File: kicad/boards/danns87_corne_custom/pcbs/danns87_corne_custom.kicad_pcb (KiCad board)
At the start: 2 copper layers, 130.4 x 81.3 mm, 46 parts

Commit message: danns87_corne_custom: PCB tracks added, DRC passes with warnings, and, I think, ready for mfg
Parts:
- removed ?: , Button_Switch_SMD:SW_SPDT_PCM12
- removed ?: , Button_Switch_SMD:SW_SPST_UXCELL
- added S22: , Button_Switch_SMD:SW_SPST_UXCELL, F.Cu at (130.8, -10.6)
- added T1: , Button_Switch_SMD:SW_SPDT_PCM12, F.Cu at (126.9, -49.7)
- gave numbers to parts that had none: 1
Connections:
- D10 pad 1: middle_bottom -> P6
- D10 pad 2: P6 -> middle_bottom
- D11 pad 1: middle_home -> P5
- D11 pad 2: P5 -> middle_home
- D12 pad 1: middle_top -> P4
- D12 pad 2: P4 -> middle_top
- D13 pad 1: index_bottom -> P6
- D13 pad 2: P6 -> index_bottom
- D14 pad 2: P5 -> index_home
- D15 pad 2: P4 -> index_top
- D16 pad 2: P6 -> inner_bottom
- D17 pad 1: inner_home -> P5
- D17 pad 2: P5 -> inner_home
- D19 pad 1: near_thumb -> P7
- D19 pad 2: P7 -> near_thumb
- D20 pad 1: home_thumb -> P7
- D20 pad 2: P7 -> home_thumb
- D21 pad 2: P7 -> far_thumb
- D3 pad 1: outer_top -> P4
- D3 pad 2: P4 -> outer_top
- D4 pad 1: pinky_bottom -> P6
- D5 pad 1: pinky_home -> P5
- D5 pad 2: P5 -> pinky_home
- D6 pad 1: pinky_top -> P4
- D6 pad 2: P4 -> pinky_top
- D7 pad 1: ring_bottom -> P6
- D8 pad 1: ring_home -> P5
- D8 pad 2: P5 -> ring_home
- D9 pad 2: P4 -> ring_top
- S1 pad 2: P14 -> P21
- S2 pad 2: P14 -> P21
- S3 pad 2: P14 -> P21
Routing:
- net P6: track 0.00 -> 244.0 mm, vias 0 -> 2
- net P18: track 0.00 -> 213.0 mm, vias 0 -> 5
- net P21: track 0.00 -> 195.5 mm, vias 0 -> 2
- net P20: track 0.00 -> 177.8 mm, vias 0 -> 4
- net P19: track 0.00 -> 174.1 mm, vias 0 -> 1
- net P15: track 0.00 -> 169.3 mm, vias 0 -> 3
- net P14: track 0.00 -> 167.5 mm, vias 0 -> 4
- net P4: track 0.00 -> 149.5 mm, vias 0 -> 1
- net P5: track 0.00 -> 145.8 mm
- net P7: track 0.00 -> 100.6 mm
- net GND: track 0.00 -> 91.0 mm, vias 0 -> 2
- net pos: track 0.00 -> 89.8 mm, vias 0 -> 2
- net RST: track 0.00 -> 44.1 mm, vias 0 -> 1
- net near_thumb: track 0.00 -> 37.1 mm
- net inner_top: track 0.00 -> 34.4 mm
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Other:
- board size 130.4 x 81.3 mm -> 131.4 x 82 mm
- net class Default removed

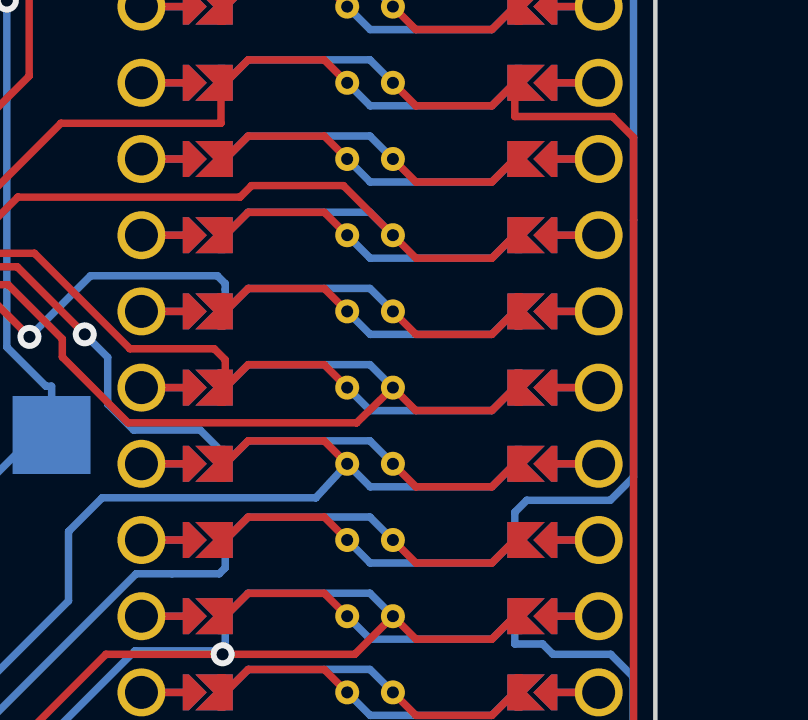
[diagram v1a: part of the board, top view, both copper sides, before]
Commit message: danns87_corne_custom: Added JLC silk screen order number placeholder
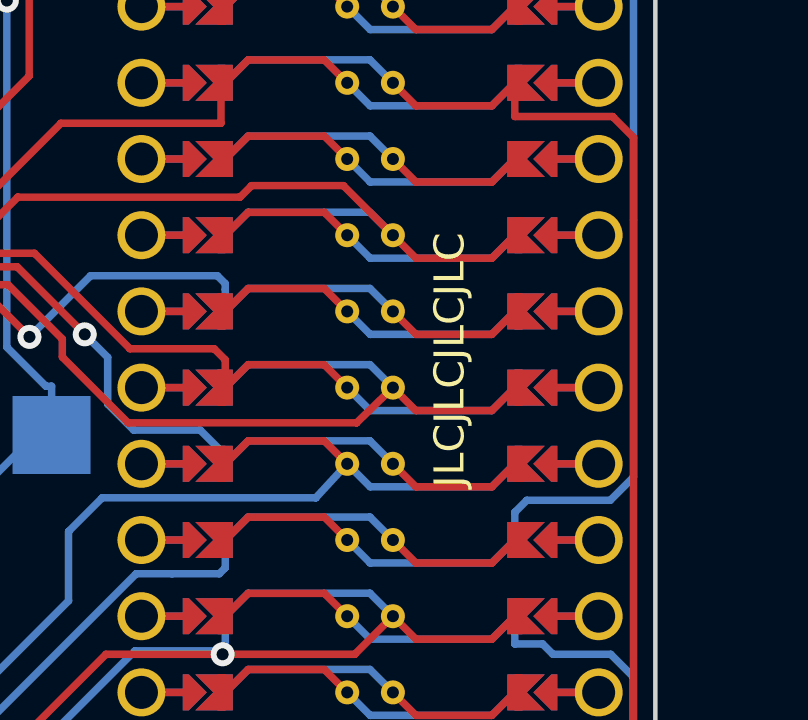
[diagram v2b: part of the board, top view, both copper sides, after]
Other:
- board text added: "JLCJLCJLCJLC"
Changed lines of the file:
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@@
       (outputformat 1)
       (mirror false)
-      (drillshape 1)
+      (drillshape 0)
       (scaleselection 1)
-      (outputdirectory "")
+      (outputdirectory "gerber/")
     )
   )
@@
   (gr_line (start 136.4 -5.4) (end 136.4 -49.9) (layer "Edge.Cuts") (width 0.15))
   (gr_arc (start 134.4 -51.9) (mid 135.814214 -51.314214) (end 136.4 -49.9) (layer "Edge.Cuts") (width 0.15))
+  (gr_text "JLCJLCJLCJLC" (at 129.54 -31.75 90) (layer "F.SilkS")
+    (effects (font (size 1 1) (thickness 0.15)))
+  )
   (segment (start 20.3908 -5.0658) (end 20.3908 3.3339) (width 0.25) (layer "F.Cu") (net 1))
   (segment (start 21.81 5) (end 19.65 5) (width 0.25) (layer "F.Cu") (net 1))

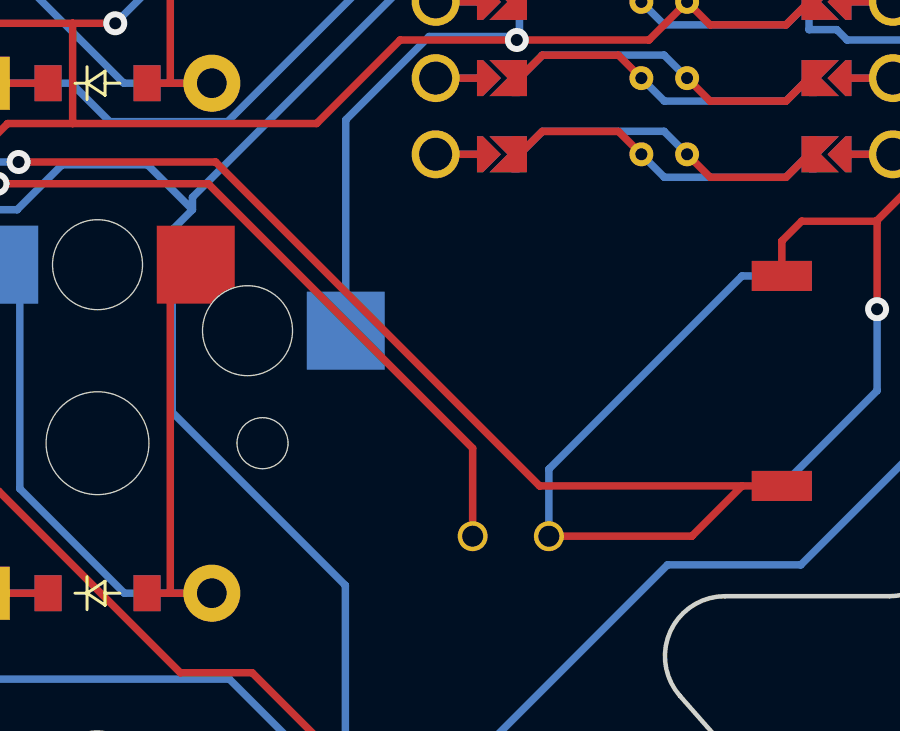
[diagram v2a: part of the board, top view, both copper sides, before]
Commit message: danns87_corne_custom: Increase JST drill hole to 0.8mm and shift in X axis to avoid collision with microcontroller legs
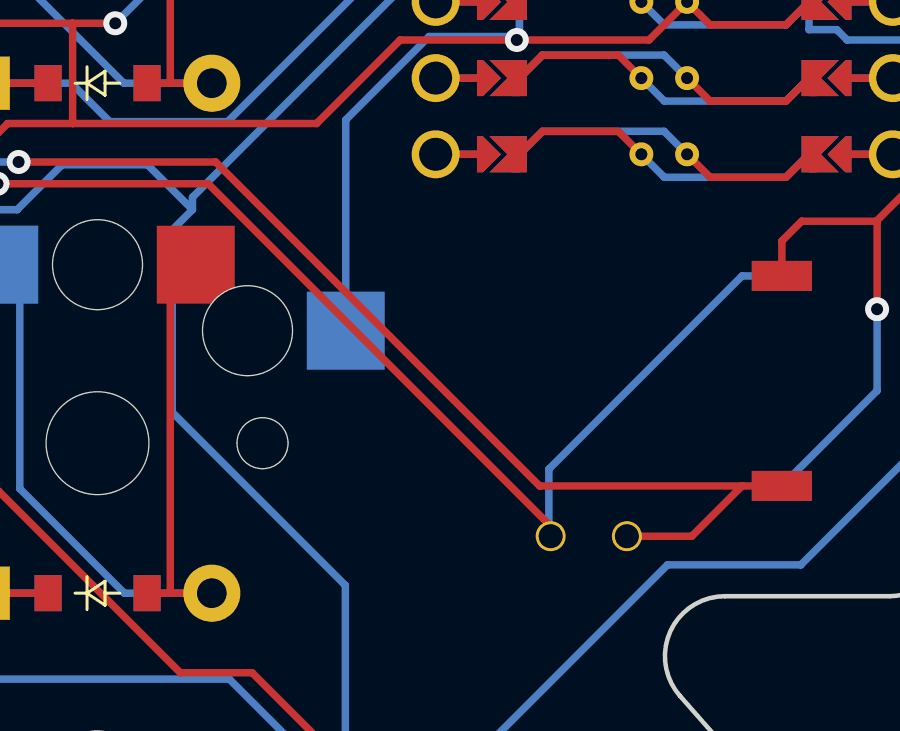
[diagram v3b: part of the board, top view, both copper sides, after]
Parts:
- moved PAD1 2.60 mm to (124.4, -5.40)
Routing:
- net GND: track 91.0 -> 88.4 mm
- net pos: track 89.8 -> 90.9 mm
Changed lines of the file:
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@@
   (net 44 "pos")
   (footprint "lib:bat2p54" (layer "F.Cu")
-    (at 121.775 -5.4 90)
+    (at 124.375 -5.4 90)
     (attr through_hole)
     (fp_text reference "PAD1" (at 0 0) (layer "F.SilkS") hide
       (effects (font (size 1.27 1.27) (thickness 0.15)))
     )
-    (fp_text value "" (at 0 0 90) (layer "F.SilkS")
+    (fp_text value "" (at -2.86 0.145 90) (layer "F.SilkS")
       (effects (font (size 1.27 1.27) (thickness 0.15)))
     )
-    (pad "1" thru_hole circle locked (at 0 -1.27 90) (size 1 1) (drill 0.7) (layers *.Cu *.SilkS *.Mask)
+    (pad "1" thru_hole circle (at 0 -1.27 90) (size 1 1) (drill 0.8) (layers *.Cu *.SilkS *.Mask)
       (net 44 "pos"))
-    (pad "2" thru_hole circle locked (at 0 1.27 90) (size 1 1) (drill 0.7) (layers *.Cu *.SilkS *.Mask)
+    (pad "2" thru_hole circle (at 0 1.27 90) (size 1 1) (drill 0.8) (layers *.Cu *.SilkS *.Mask)
       (net 33 "GND"))
   )
@@
   (segment (start 127.64 -46.082) (end 127.652 -46.07) (width 0.25) (layer "B.Cu") (net 32))
   (segment (start 127.64 -48.245) (end 127.64 -46.082) (width 0.25) (layer "B.Cu") (net 32))
-  (segment (start 123.045 -5.4) (end 127.8097 -5.4) (width 0.25) (layer "F.Cu") (net 33))
   (segment (start 121.92 -39.6406) (end 116.585 -39.6406) (width 0.25) (layer "F.Cu") (net 33))
   (segment (start 131.716 -43.53) (end 131.6387 -43.53) (width 0.25) (layer "F.Cu") (net 33))
@@
   (segment (start 116.585 -39.6406) (end 114.0538 -37.1094) (width 0.25) (layer "F.Cu") (net 33))
   (segment (start 130.81 -7.075) (end 129.4847 -7.075) (width 0.25) (layer "F.Cu") (net 33))
+  (segment (start 125.645 -5.4) (end 127.8097 -5.4) (width 0.25) (layer "F.Cu") (net 33))
   (segment (start 121.92 -39.6406) (end 121.92 -40.99) (width 0.25) (layer "F.Cu") (net 33))
-  (segment (start 127.8097 -5.4) (end 129.4847 -7.075) (width 0.25) (layer "F.Cu") (net 33))
   (segment (start 121.92 -40.99) (end 122.064 -40.99) (width 0.25) (layer "F.Cu") (net 33))
   (segment (start 129.4847 -7.075) (end 122.7353 -7.075) (width 0.25) (layer "F.Cu") (net 33))
+  (segment (start 127.8097 -5.4) (end 129.4847 -7.075) (width 0.25) (layer "F.Cu") (net 33))
   (via (at 114.0538 -37.1094) (size 0.8) (drill 0.4) (layers "F.Cu" "B.Cu") (net 33))
   (via (at 105.3697 -17.8734) (size 0.8) (drill 0.4) (layers "F.Cu" "B.Cu") (net 33))
@@
   (segment (start 133.985 -12.9664) (end 133.985 -10.25) (width 0.25) (layer "B.Cu") (net 34))
   (segment (start 127 -49.53) (end 127 -50.2999) (width 0.25) (layer "F.Cu") (net 44))
+  (segment (start 111.6889 -17.1481) (end 104.6651 -17.1481) (width 0.25) (layer "F.Cu") (net 44))
   (segment (start 128.285 -48.245) (end 127 -49.53) (width 0.25) (layer "F.Cu") (net 44))
-  (segment (start 120.505 -8.332) (end 111.6889 -17.1481) (width 0.25) (layer "F.Cu") (net 44))
   (segment (start 129.14 -48.245) (end 128.285 -48.245) (width 0.25) (layer "F.Cu") (net 44))
-  (segment (start 120.505 -5.4) (end 120.505 -8.332) (width 0.25) (layer "F.Cu") (net 44))
-  (segment (start 111.6889 -17.1481) (end 104.6651 -17.1481) (width 0.25) (layer "F.Cu") (net 44))
+  (segment (start 123.105 -5.732) (end 111.6889 -17.1481) (width 0.25) (layer "F.Cu") (net 44))
+  (segment (start 123.105 -5.4) (end 123.105 -5.732) (width 0.25) (layer "F.Cu") (net 44))
   (via (at 104.6651 -17.1481) (size 0.8) (drill 0.4) (layers "F.Cu" "B.Cu") (net 44))
   (via (at 127 -50.2999) (size 0.8) (drill 0.4) (layers "F.Cu" "B.Cu") (net 44))
